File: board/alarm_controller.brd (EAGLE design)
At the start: 90 x 65 mm, 144 parts, among them IC3 AT24C, X1 RJ45-8L21-S, X2 RJ45-8L21-S

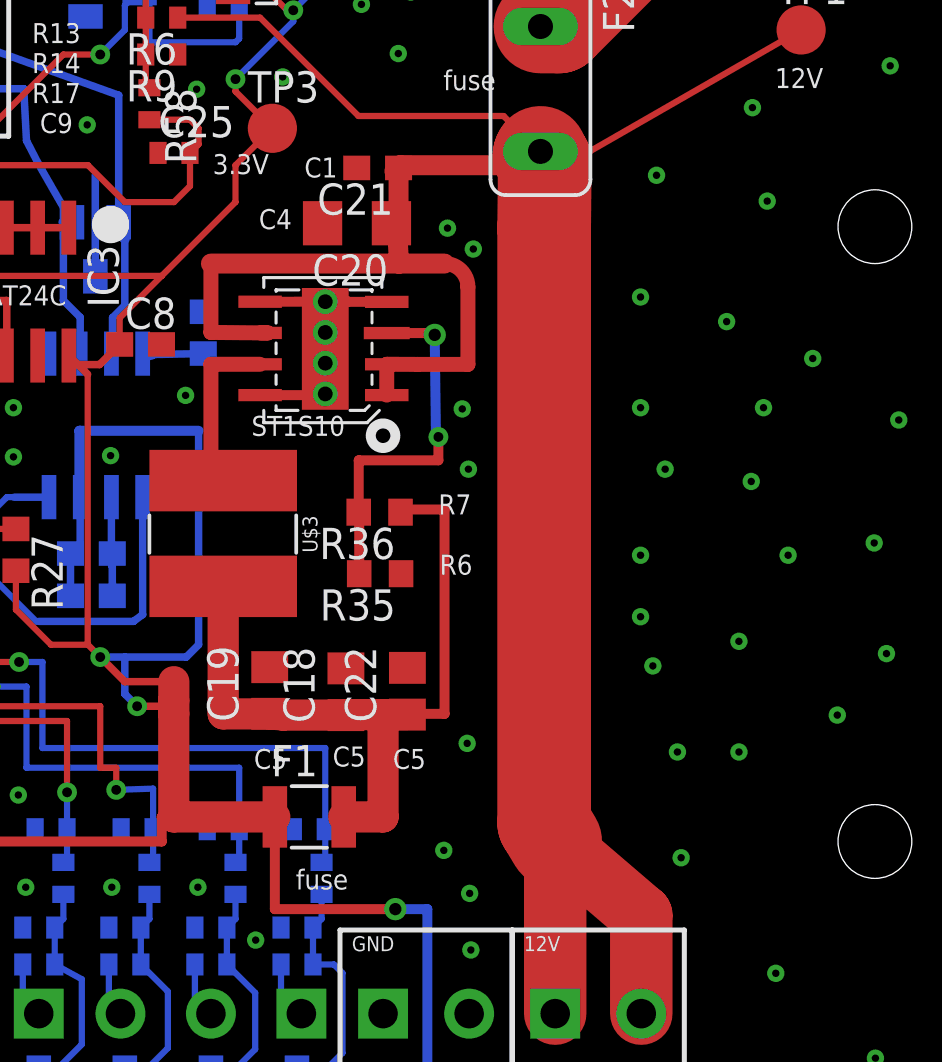
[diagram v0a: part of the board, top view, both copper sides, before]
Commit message: change to premade power supply
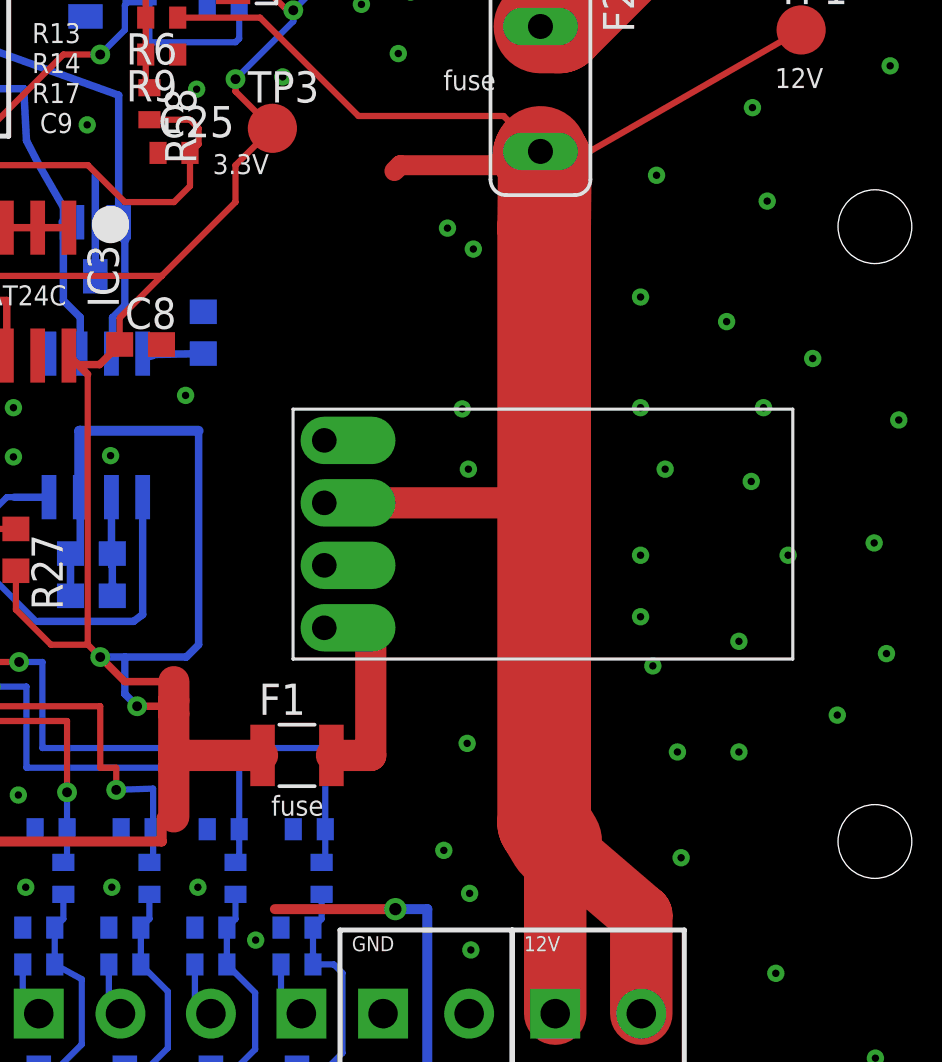
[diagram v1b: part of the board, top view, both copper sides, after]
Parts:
- removed C18, C19, C22: 22uF, rcl:C0805
- removed C20: 4,7u, rcl:C1206
- removed C21: 100n, rcl:C0603
- removed R35: 15k, rcl:R0603
- removed R36: 47k, rcl:R0603
- removed U$2: ST1S10, lcd:POWERSO-8
- removed U$3: 4,7uH, lcd:0504
- added U$4: HW-613, components:HW-613
- moved F1 2.55 mm to (62.5, 23.5)
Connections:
- removed net N$13: C18.1, C19.1, C22.1, F1.2, R36.1, U$3.2
- removed net N$7: U$2.7, U$3.1
- net +12V: now also U$4.IN; no longer C20.1, C21.1, U$2.1, U$2.2, U$2.6
- net GND: now also U$4.GND; no longer C18.2, C19.2, C20.2, C21.2, C22.2, R35.1, U$2.4, U$2.5, U$2.8, U$2.9
- net N$3: now also F1.2, U$4.OUT; no longer R35.2, R36.2, U$2.3
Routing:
- net N$13: track 37.8 -> 0.00 mm
- net +12V: track 117.2 -> 97.5 mm
- net GND: track 75.4 -> 62.0 mm, vias 185 -> 181
- net +3V3: track 410.0 -> 401.2 mm
- net N$7: track 8.16 -> 0.00 mm
- net N$3: track 15.0 -> 8.68 mm, vias 2 -> 0
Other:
- board text removed: "C4"
- board text removed: "C5"
- board text removed: "R6"
- board text removed: "R7"
- board text removed: "ST1S10"

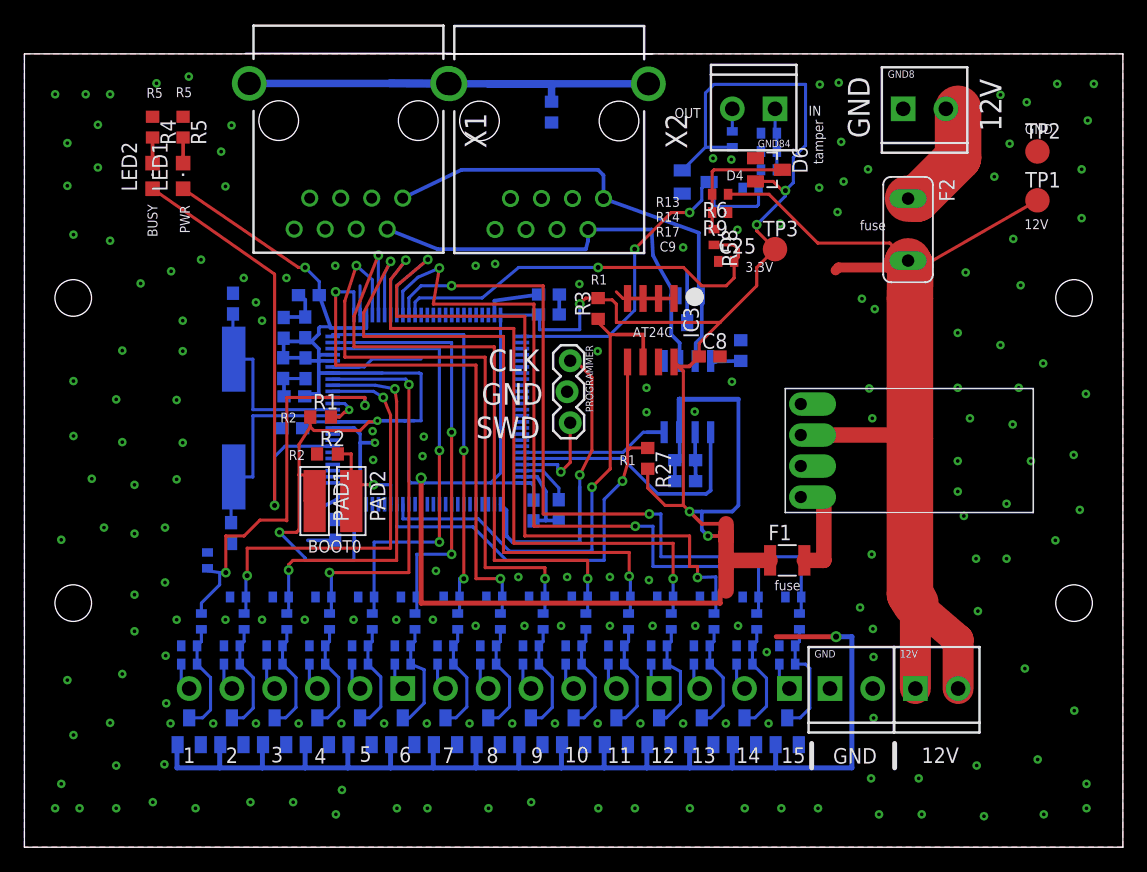
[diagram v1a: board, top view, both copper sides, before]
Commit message: change mounting to lib version
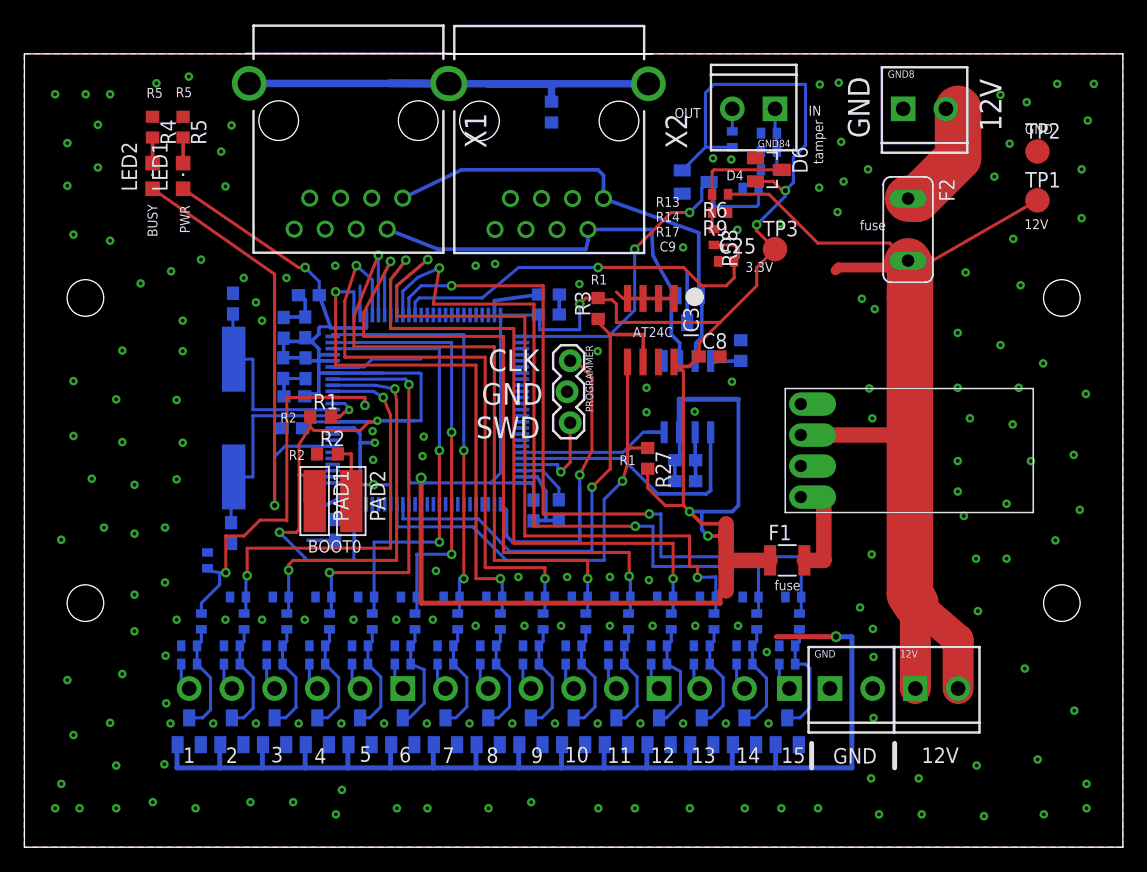
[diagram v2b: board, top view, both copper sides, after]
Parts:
- added U$2, U$3: (no value), mounting:DIN-MOUNT-2-HOLE
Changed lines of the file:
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@@
 <text x="14.04" y="36.45" size="0.8128" layer="122" rot="MR270">8Mhz</text>
 <text x="61.82" y="40.25" size="0.6096" layer="122" rot="MR0">slope</text>
-<hole x="4" y="20" drill="3"/>
-<hole x="4" y="45" drill="3"/>
-<hole x="86" y="20" drill="3"/>
-<hole x="86" y="45" drill="3"/>
 <text x="56.5664" y="31.6656" size="0.8128" layer="122" rot="MR0" align="center">C1</text>
 <text x="56.74" y="29.9444" size="0.8128" layer="122" rot="MR0" align="center">C2</text>
@@
 </element>
 <element name="U$4" library="components" package="HW-613" value="HW-613" x="72.5" y="32.5"/>
+<element name="U$2" library="mounting" package="DIN-MOUNT-2-HOLE" value="" x="5" y="32.5"/>
+<element name="U$3" library="mounting" package="DIN-MOUNT-2-HOLE" value="" x="85" y="32.5"/>
 </elements>
 <signals>
@@
 </signal>
 </signals>
-<errors>
-</errors>
 </board>
 </drawing>

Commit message: board - minor adjustments
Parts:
- moved LED2 7.50 mm to (4.50, 59.5), turned to 180 degrees
- moved LED1 7.11 mm to (7.50, 59.5), turned to 180 degrees
- moved R4 6.95 mm to (4.50, 55.5), turned to 90 degrees
- moved R5 6.52 mm to (7.50, 55.5), turned to 90 degrees
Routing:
- net +3V3: track 401.2 -> 420.3 mm
- net BUSY_LED: track 40.3 -> 57.6 mm
- net +12V: track 97.5 -> 92.9 mm
- net GND: vias 181 -> 182
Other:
- board text added: "2020.05.08 v1.2"
- board text added: "HW-613"
